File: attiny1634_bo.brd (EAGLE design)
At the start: 49.5 x 22.2 mm, 11 parts, among them J1 AVR_SPI_PRG_6NS, Y1 12MHz

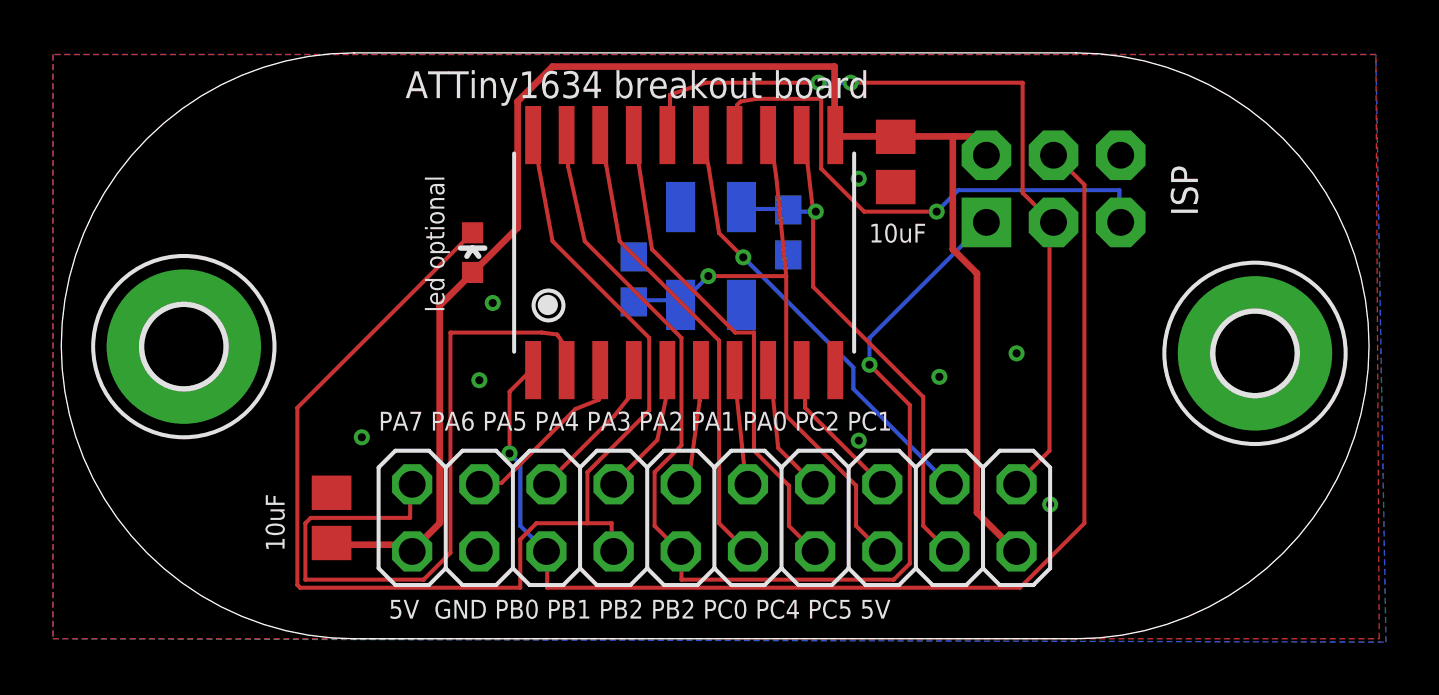
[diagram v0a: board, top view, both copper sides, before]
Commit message: adjusted xtal position
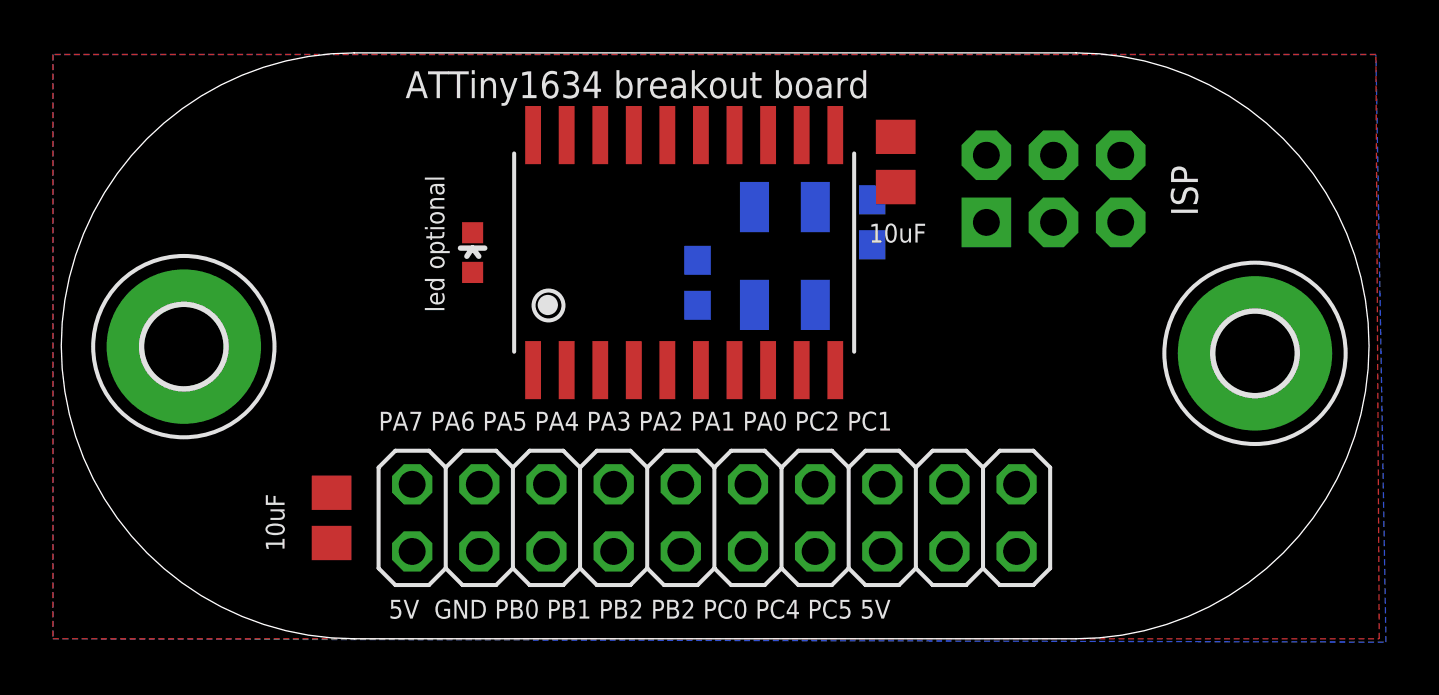
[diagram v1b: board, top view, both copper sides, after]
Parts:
- moved CX1 3.20 mm to (31.0, 15.7), turned to 270 degrees
- moved Y1 2.79 mm to (27.7, 14.5)
- moved CX0 2.42 mm to (24.4, 13.5)
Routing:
- net +5V: track 60.5 -> 0.00 mm
- net PB1/ADC6/RX1: track 48.4 -> 0.00 mm
- net PB0/MOSI/TX0/ADC5: track 45.0 -> 0.00 mm, vias 1 -> 0
- net PB2/ADC7/TX1: track 43.6 -> 0.00 mm, vias 1 -> 0
- net PC1/SCL/ADC10: track 31.3 -> 0.00 mm, vias 2 -> 0
- net PA7: track 27.2 -> 0.00 mm
- net PC4/XTAL2: track 23.7 -> 0.00 mm, vias 1 -> 0
- net PC5/XTAL1: track 20.9 -> 0.00 mm, vias 1 -> 0
- net PC3/-RESET: track 20.6 -> 0.00 mm, vias 1 -> 0
- net PC0/ADC9/OC0A: track 18.8 -> 0.00 mm
- net PB3/ADC8/OC1A: track 17.8 -> 0.00 mm
- net PC2/ADC11: track 16.9 -> 0.00 mm, vias 1 -> 0
- net PA6: track 6.91 -> 0.00 mm
- net PA0: track 5.60 -> 0.00 mm
- net PA5: track 5.60 -> 0.00 mm
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
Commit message: pre-routed the clock
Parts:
- moved CX1 1.42 mm to (30.7, 17.1)
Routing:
- net PC4/XTAL2: track 0.00 -> 8.79 mm, vias 0 -> 1
- net PC5/XTAL1: track 0.00 -> 4.68 mm, vias 0 -> 1
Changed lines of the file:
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@@
 </element>
 <element name="CX0" library="rcl" package="C0603" value="22pF" x="24.384" y="13.462" smashed="yes" rot="MR270"/>
-<element name="CX1" library="rcl" package="C0603" value="22pF" x="30.988" y="15.748" smashed="yes" rot="MR270"/>
+<element name="CX1" library="rcl" package="C0603" value="22pF" x="30.734" y="17.145" smashed="yes" rot="MR270"/>
 <element name="Y1" library="SparkFun-FreqCtrl" package="CRYSTAL-SMD-5X3" value="12MHz" x="27.686" y="14.478" smashed="yes" rot="MR270"/>
 <element name="H1" library="holes" package="3,0-PAD" value="MOUNT-PAD-ROUND3.0" x="4.953" y="11.049"/>
@@
 <contactref element="Y1" pad="1"/>
 <contactref element="JP1" pad="4"/>
-<wire x1="28.836" y1="16.328" x2="28.321" y2="19.05" width="0" layer="19" extent="1-16"/>
-<wire x1="30.988" y1="14.898" x2="28.836" y2="16.328" width="0" layer="19" extent="16-16"/>
-<wire x1="33.909" y1="3.302" x2="30.988" y2="14.898" width="0" layer="19" extent="16-16"/>
+<wire x1="28.321" y1="19.05" x2="28.702" y2="16.891" width="0.1524" layer="1"/>
+<via x="28.702" y="16.891" extent="1-16" drill="0.3048"/>
+<wire x1="28.702" y1="16.891" x2="28.829" y2="16.335" width="0.1524" layer="16"/>
+<wire x1="28.829" y1="16.335" x2="28.836" y2="16.328" width="0.1524" layer="16"/>
+<wire x1="30.734" y1="16.295" x2="28.869" y2="16.295" width="0.1524" layer="16"/>
+<wire x1="28.869" y1="16.295" x2="28.836" y2="16.328" width="0.1524" layer="16"/>
+<wire x1="33.909" y1="3.302" x2="30.734" y2="16.295" width="0" layer="19" extent="16-16"/>
 </signal>
 <signal name="PC4/XTAL2">
@@
 <contactref element="Y1" pad="3"/>
 <contactref element="JP1" pad="6"/>
-<wire x1="26.536" y1="12.628" x2="27.051" y2="19.05" width="0" layer="19" extent="1-16"/>
-<wire x1="24.384" y1="12.612" x2="26.536" y2="12.628" width="0" layer="19" extent="16-16"/>
-<wire x1="31.369" y1="3.302" x2="26.536" y2="12.628" width="0" layer="19" extent="16-16"/>
+<wire x1="27.051" y1="19.05" x2="27.051" y2="13.589" width="0.1524" layer="1"/>
+<wire x1="27.051" y1="13.589" x2="26.67" y2="13.208" width="0.1524" layer="1"/>
+<via x="26.67" y="13.208" extent="1-16" drill="0.3048"/>
+<wire x1="26.67" y1="13.208" x2="26.67" y2="12.762" width="0.1524" layer="16"/>
+<wire x1="26.67" y1="12.762" x2="26.536" y2="12.628" width="0.1524" layer="16"/>
+<wire x1="26.536" y1="12.628" x2="24.4" y2="12.628" width="0.1524" layer="16"/>
+<wire x1="24.4" y1="12.628" x2="24.384" y2="12.612" width="0.1524" layer="16"/>
+<wire x1="26.536" y1="12.628" x2="31.369" y2="3.302" width="0" layer="19" extent="16-16"/>
 </signal>
 <signal name="PA0">

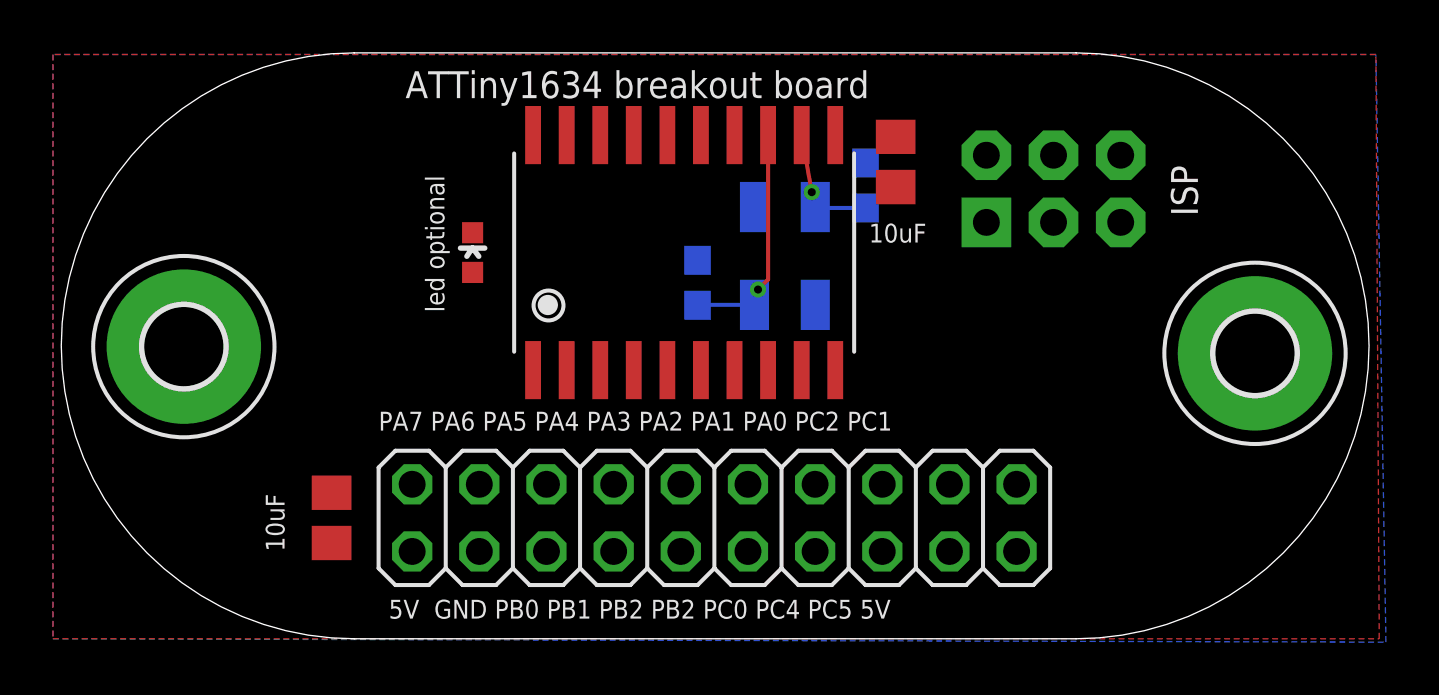
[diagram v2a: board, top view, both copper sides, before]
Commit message: freeroute.net autorouted (and some vias added)
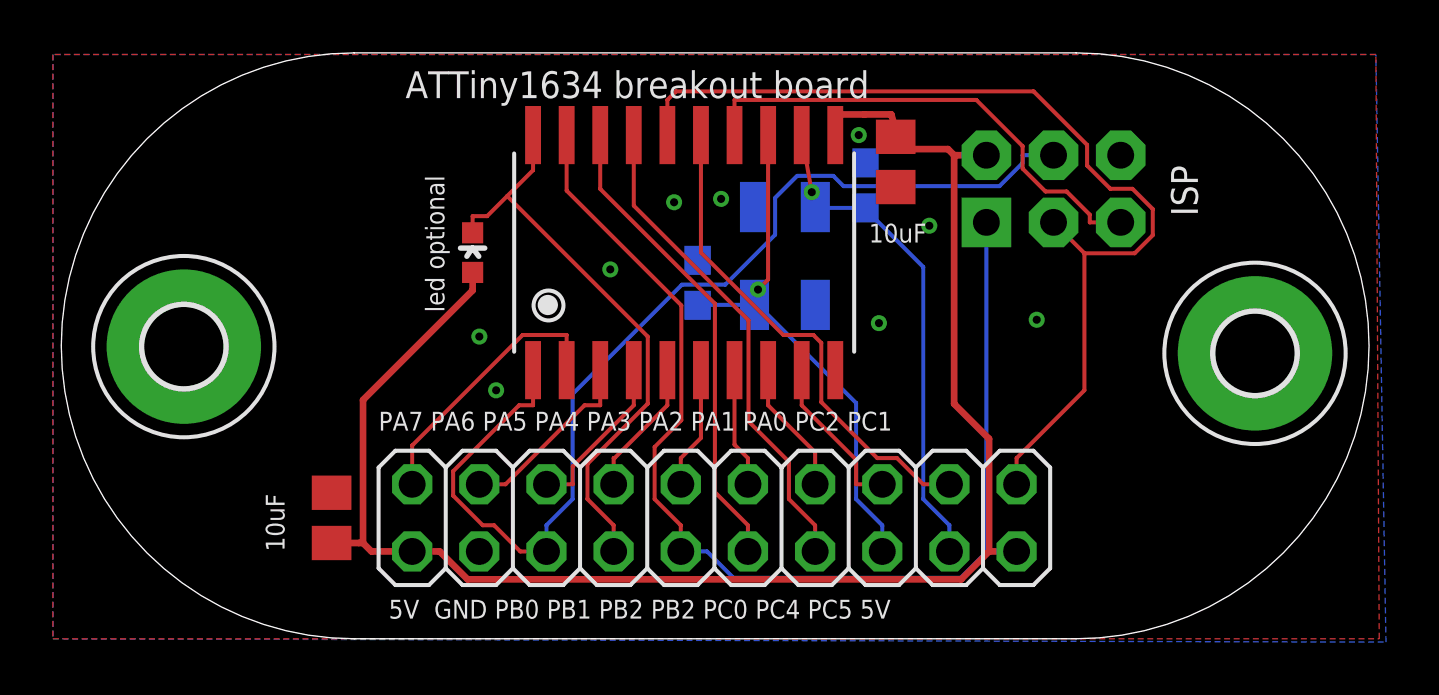
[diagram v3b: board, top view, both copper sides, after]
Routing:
- net +5V: track 0.00 -> 62.5 mm
- net PB2/ADC7/TX1: track 0.00 -> 43.2 mm
- net PB0/MOSI/TX0/ADC5: track 0.00 -> 40.3 mm
- net PC1/SCL/ADC10: track 0.00 -> 37.4 mm
- net PB1/ADC6/RX1: track 0.00 -> 22.0 mm
- net PC2/ADC11: track 0.00 -> 18.8 mm
- net PC0/ADC9/OC0A: track 0.00 -> 18.6 mm
- net PC3/-RESET: track 0.00 -> 18.5 mm
- net PB3/ADC8/OC1A: track 0.00 -> 18.1 mm
- net PC5/XTAL1: track 4.68 -> 19.0 mm
- net PC4/XTAL2: track 8.79 -> 20.2 mm
- net PA7: track 0.00 -> 10.4 mm
- net PA6: track 0.00 -> 7.14 mm
- net PA5: track 0.00 -> 6.27 mm
- net PA0: track 0.00 -> 6.16 mm
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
